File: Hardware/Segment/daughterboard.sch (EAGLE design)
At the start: 49 parts, among them IC1 PBQ79656PAPTQ1

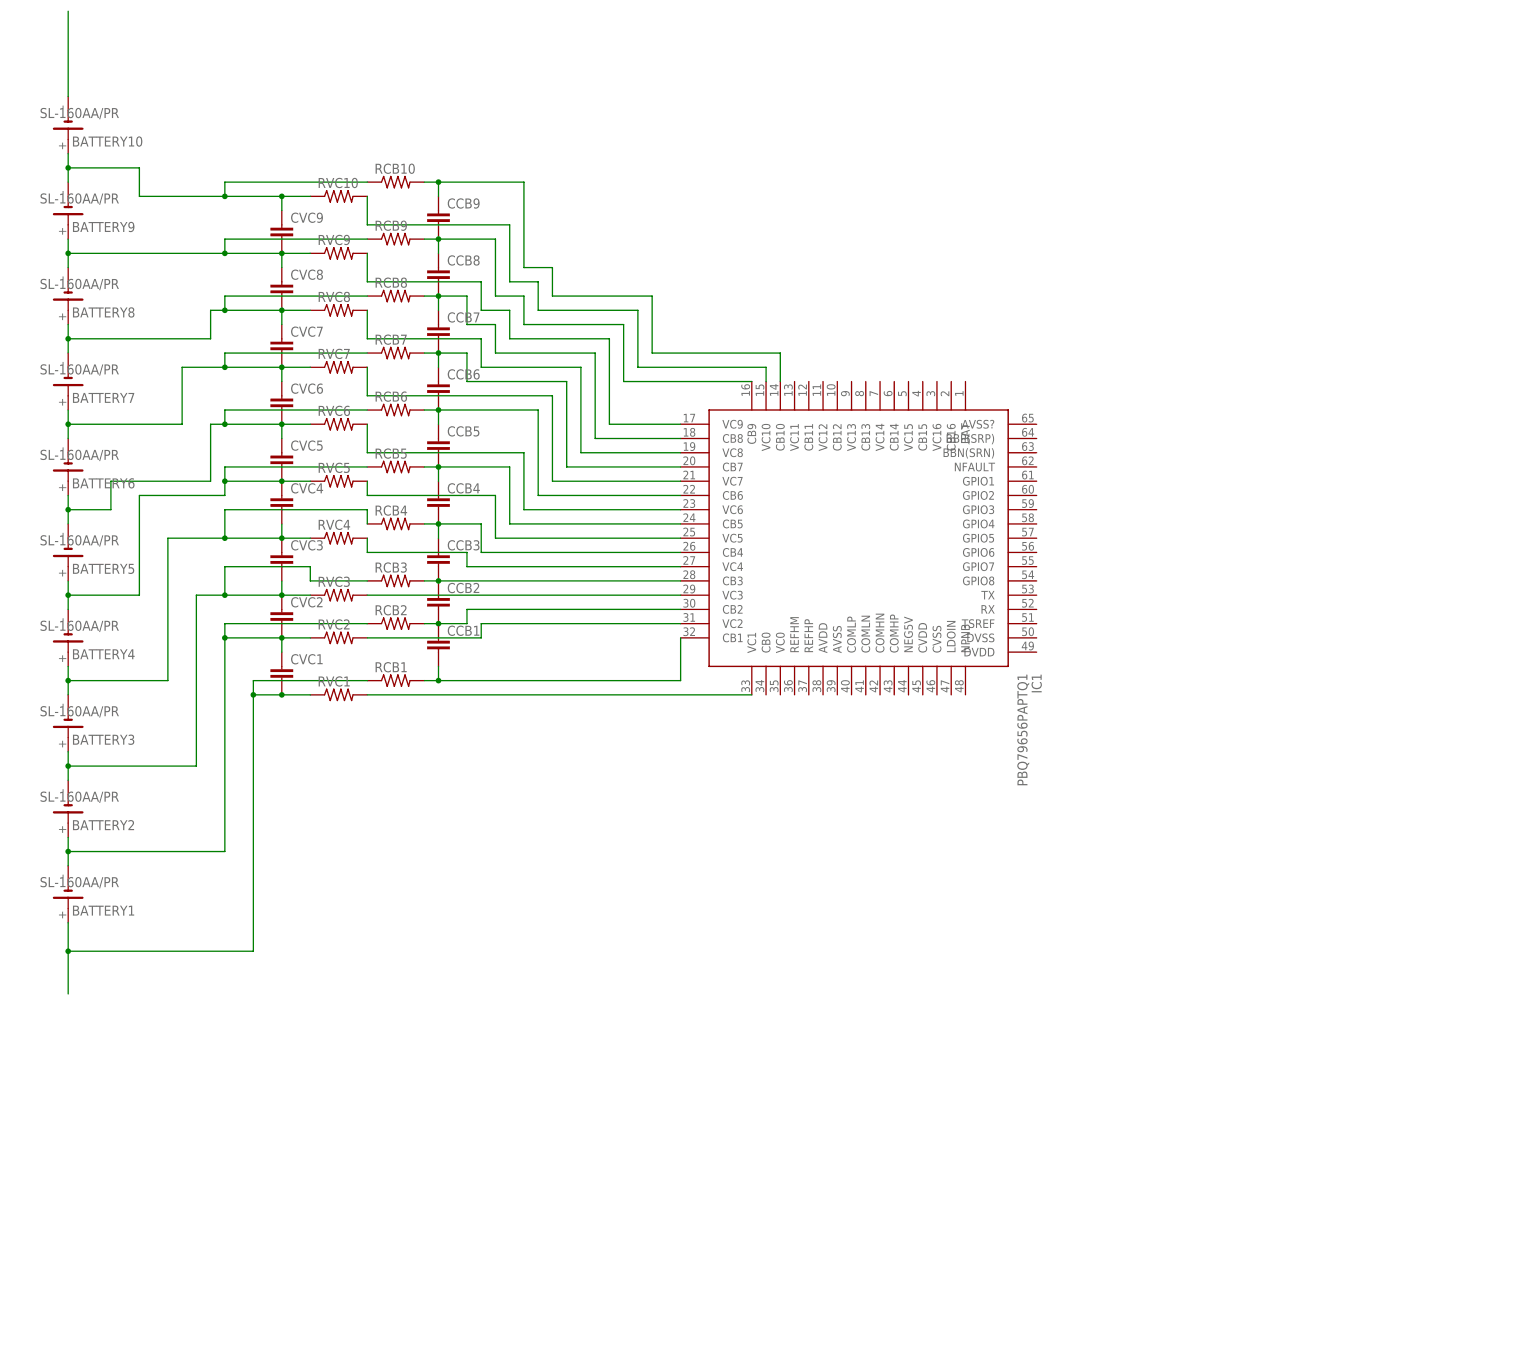
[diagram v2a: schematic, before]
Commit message: Added connections to thermistors
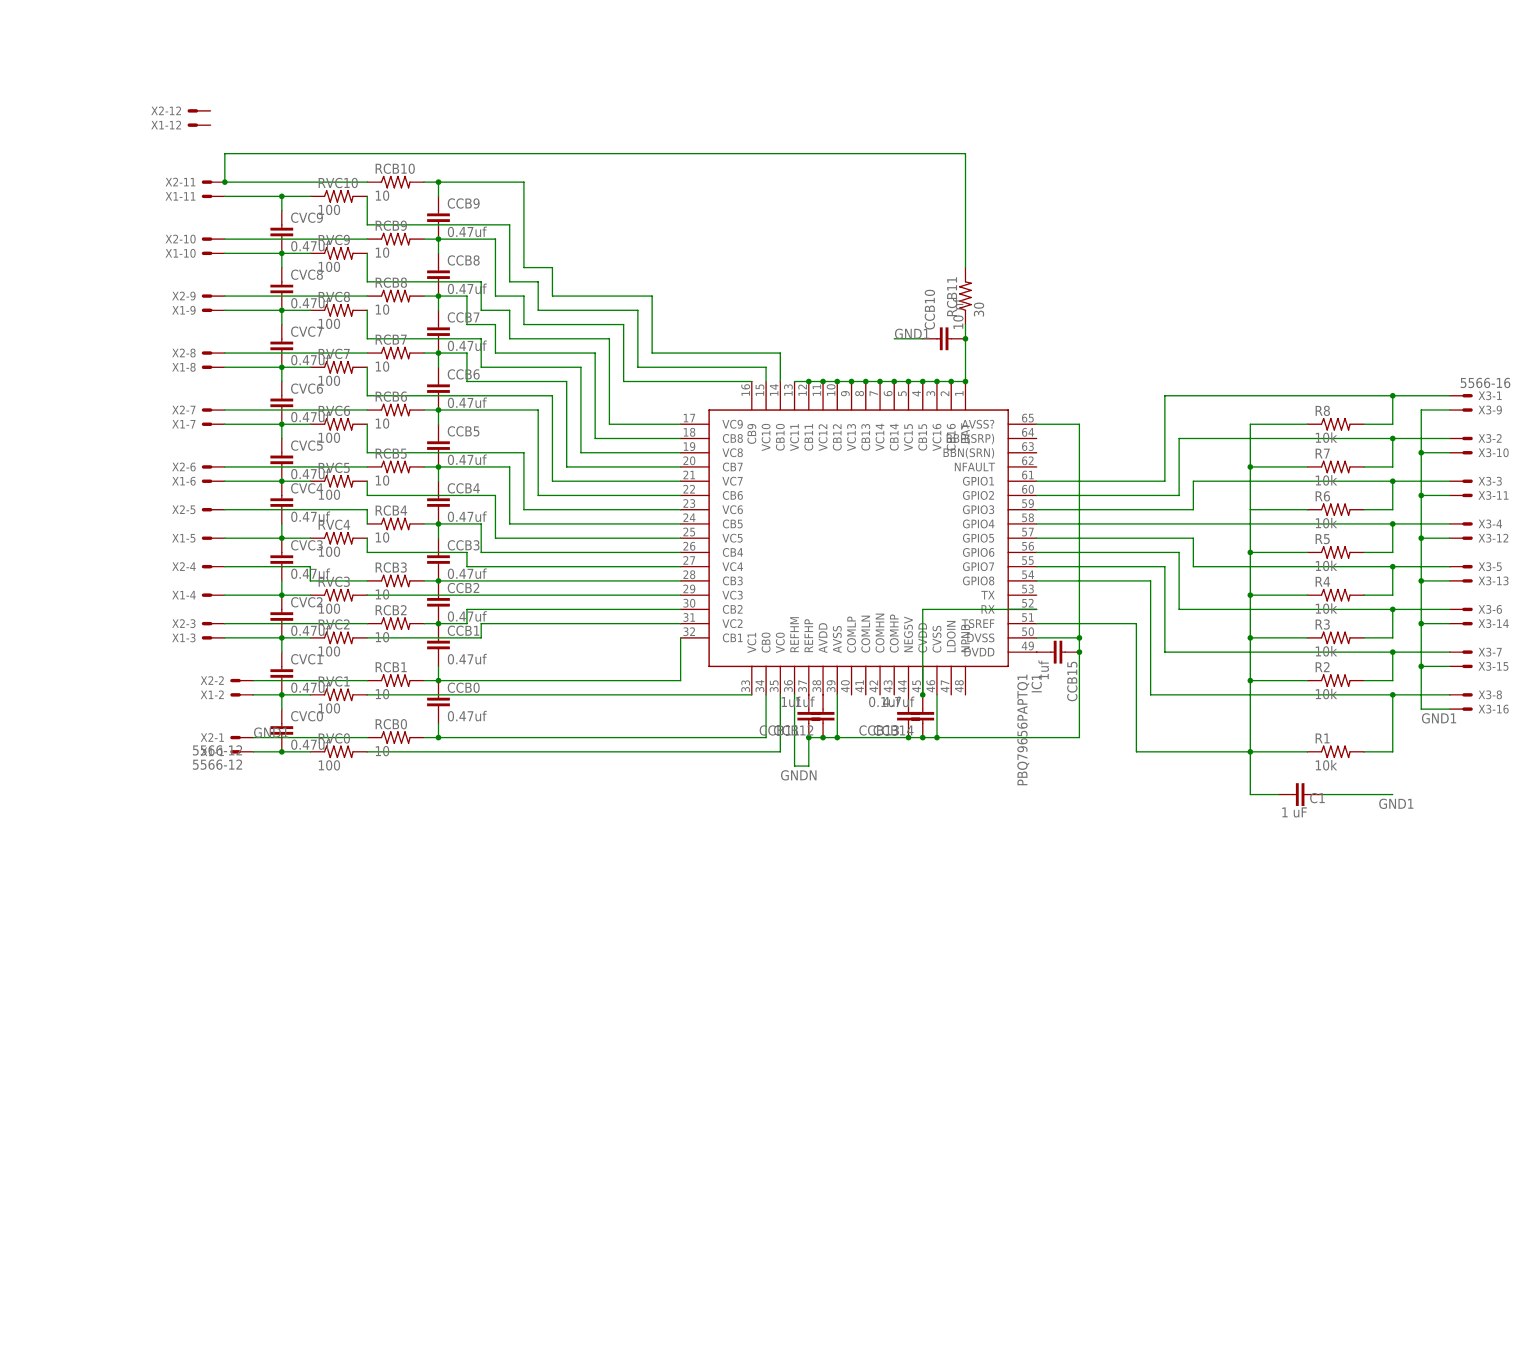
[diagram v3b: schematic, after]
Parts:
- removed BATTERY1, BATTERY10, BATTERY2, BATTERY3, BATTERY4, BATTERY5, BATTERY6, BATTERY7, BATTERY8, BATTERY9: SL-160AA/PR, battery:SL-160AA/PR
- added C1: 1 uF, capacitor-wima:C2.5/2
- added CCB0, CVC0: 0.47uf, capacitor-wima:C2.5/2
- added CCB10: 10 nf, capacitor-wima:C2.5/2
- added CCB11, CCB12, CCB15: 1uf, capacitor-wima:C2.5/2
- added CCB13: 0.1uf, capacitor-wima:C2.5/2
- added CCB14: 4.7uf, capacitor-wima:C2.5/2
- added R1, R2, R3, R4, R5, R6, R7, R8: 10k, rcl:R-US_R0603
- added RCB0: 10, rcl:R-US_R0603
- added RCB11: 30, rcl:R-US_R0603
- added RVC0: 100, rcl:R-US_R0603
- added X1, X2: 5566-12, con-molex:5566-12
- added X3: 5566-16, con-molex:5566-16
- CCB1, CCB2, CCB3, CCB4, CCB5, CCB6, CCB7, CCB8, CCB9, CVC1, CVC2, CVC3, CVC4, CVC5, CVC6, CVC7, CVC8, CVC9: value (none) -> 0.47uf
- RCB1, RCB10, RCB2, RCB3, RCB4, RCB5, RCB6, RCB7, RCB8, RCB9: value (none) -> 10
- RVC1, RVC10, RVC2, RVC3, RVC4, RVC5, RVC6, RVC7, RVC8, RVC9: value (none) -> 100
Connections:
- new net GND1: C1.1, CCB10.1, RCB0.1, X2-1.S, X3-10.S, X3-11.S, X3-12.S, X3-13.S, X3-14.S, X3-15.S, X3-16.S, X3-9.S
- new net GNDN: CCB11.1, CCB12.1, CCB13.1, CCB14.1, CCB15.1, IC1.AVSS, IC1.AVSS?, IC1.CVSS, IC1.DVSS, IC1.REFHM
- new net N$25: CCB0.2, IC1.CB0, RCB0.2
- new net N$33: CCB11.2, IC1.REFHP
- new net N$34: CVC0.2, RVC0.1, X1-1.S
- new net N$35: CVC0.1, CVC1.2, RVC1.1, X1-2.S
- new net N$36: CVC1.1, CVC2.2, RVC2.1, X1-3.S
- new net N$37: CVC2.1, CVC3.2, RVC3.1, X1-4.S
- new net N$38: CVC3.1, CVC4.2, RVC4.1, X1-5.S
- new net N$39: CVC4.1, CVC5.2, RVC5.1, X1-6.S
- new net N$40: CVC5.1, CVC6.2, RVC6.1, X1-7.S
- new net N$41: CVC6.1, CVC7.2, RVC7.1, X1-8.S
- new net N$42: CVC7.1, CVC8.2, RVC8.1, X1-9.S
- new net N$43: CVC8.1, CVC9.2, RVC9.1, X1-10.S
- new net N$44: CVC9.1, RVC10.1, X1-11.S
- new net N$45: CCB10.2, IC1.BAT, IC1.CB11, IC1.CB12, IC1.CB13, IC1.CB14, IC1.CB15, IC1.CB16, IC1.VC11, IC1.VC12, IC1.VC13, IC1.VC14, IC1.VC15, IC1.VC16, RCB11.1
- new net N$46: CCB12.2, IC1.AVDD
- new net N$47: IC1.GPIO1, R8.2, X3-1.S
- new net N$48: CCB13.2, IC1.NEG5V
- new net N$49: CCB14.2, IC1.CVDD, IC1.RX
- new net N$50: CCB15.2, IC1.DVDD
- new net N$51: IC1.GPIO2, R7.2, X3-2.S
- new net N$52: IC1.GPIO3, R6.2, X3-3.S
- new net N$53: IC1.GPIO4, R5.2, X3-4.S
- new net N$54: IC1.GPIO5, R4.2, X3-5.S
- new net N$55: IC1.GPIO6, R3.2, X3-6.S
- new net N$56: IC1.GPIO7, R2.2, X3-7.S
- new net N$57: IC1.GPIO8, R1.2, X3-8.S
- new net N$58: C1.2, IC1.TSREF, R1.1, R2.1, R3.1, R4.1, R5.1, R6.1, R7.1, R8.1
- net N$12: now also X2-5.S; no longer BATTERY3.-, BATTERY4.+, CVC3.1, CVC4.2, RVC4.1
- net N$15: now also X2-6.S; no longer BATTERY4.-, BATTERY5.+, CVC4.1, CVC5.2, RVC5.1
- net N$18: now also X2-9.S; no longer BATTERY7.-, BATTERY8.+, CVC7.1, CVC8.2, RVC8.1
- net N$2: now also CCB0.1
- net N$21: now also X2-10.S; no longer BATTERY8.-, BATTERY9.+, CVC8.1, CVC9.2, RVC9.1
- net N$24: now also IC1.VC0, RVC0.2; no longer BATTERY10.-
- net N$27: now also X2-7.S; no longer BATTERY5.-, BATTERY6.+, CVC5.1, CVC6.2, RVC6.1
- net N$29: now also RCB11.2, X2-11.S; no longer BATTERY10.+, BATTERY9.-, CVC9.1, RVC10.1
- net N$31: now also X2-8.S; no longer BATTERY6.-, BATTERY7.+, CVC6.1, CVC7.2, RVC7.1
- net N$5: now also X2-2.S; no longer BATTERY1.+, CVC1.2, RVC1.1
- net N$6: now also X2-3.S; no longer BATTERY1.-, BATTERY2.+, CVC1.1, CVC2.2, RVC2.1
- net N$8: now also X2-4.S; no longer BATTERY2.-, BATTERY3.+, CVC2.1, CVC3.2, RVC3.1

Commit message: Part of com
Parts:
- added CCB16, CCB17: 2.2nf, capacitor-wima:C2.5/2
- added CCB18, CCB19: 220pf, capacitor-wima:C2.5/2
- added RVC11, RVC12, RVC13, RVC14: 49, rcl:R-US_R0603
- added RVC15: 1k, rcl:R-US_R0603
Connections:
- new net N$59: CCB18.1, IC1.COMHN, RVC11.2, RVC15.2
- new net N$60: CCB19.2, IC1.COMHP, RVC12.2, RVC15.1
- new net N$61: CCB16.2, RVC11.1
- new net N$62: CCB17.2, RVC12.1
- new net N$63: CCB16.1, RVC13.2
- new net N$64: CCB17.1, RVC14.2
- net GNDN: now also CCB18.2, CCB19.1
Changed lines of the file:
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@@
 <part name="R7" library="rcl" library_urn="urn:adsk.eagle:library:334" deviceset="R-US_" device="R0603" package3d_urn="urn:adsk.eagle:package:23555/3" value="10k"/>
 <part name="R8" library="rcl" library_urn="urn:adsk.eagle:library:334" deviceset="R-US_" device="R0603" package3d_urn="urn:adsk.eagle:package:23555/3" value="10k"/>
+<part name="RVC11" library="rcl" library_urn="urn:adsk.eagle:library:334" deviceset="R-US_" device="R0603" package3d_urn="urn:adsk.eagle:package:23555/3" value="49"/>
+<part name="RVC12" library="rcl" library_urn="urn:adsk.eagle:library:334" deviceset="R-US_" device="R0603" package3d_urn="urn:adsk.eagle:package:23555/3" value="49"/>
+<part name="CCB16" library="capacitor-wima" library_urn="urn:adsk.eagle:library:116" deviceset="C" device="2.5/2" package3d_urn="urn:adsk.eagle:package:5415/1" value="2.2nf"/>
+<part name="CCB17" library="capacitor-wima" library_urn="urn:adsk.eagle:library:116" deviceset="C" device="2.5/2" package3d_urn="urn:adsk.eagle:package:5415/1" value="2.2nf"/>
+<part name="RVC13" library="rcl" library_urn="urn:adsk.eagle:library:334" deviceset="R-US_" device="R0603" package3d_urn="urn:adsk.eagle:package:23555/3" value="49"/>
+<part name="RVC14" library="rcl" library_urn="urn:adsk.eagle:library:334" deviceset="R-US_" device="R0603" package3d_urn="urn:adsk.eagle:package:23555/3" value="49"/>
+<part name="RVC15" library="rcl" library_urn="urn:adsk.eagle:library:334" deviceset="R-US_" device="R0603" package3d_urn="urn:adsk.eagle:package:23555/3" value="1k"/>
+<part name="CCB18" library="capacitor-wima" library_urn="urn:adsk.eagle:library:116" deviceset="C" device="2.5/2" package3d_urn="urn:adsk.eagle:package:5415/1" value="220pf"/>
+<part name="CCB19" library="capacitor-wima" library_urn="urn:adsk.eagle:library:116" deviceset="C" device="2.5/2" package3d_urn="urn:adsk.eagle:package:5415/1" value="220pf"/>
 </parts>
 <sheets>
@@
 <attribute name="NAME" x="240.03" y="77.6986" size="1.778" layer="95"/>
 <attribute name="VALUE" x="240.03" y="72.898" size="1.778" layer="96"/>
+</instance>
+<instance part="RVC11" gate="G$1" x="162.56" y="-2.54" smashed="yes" rot="R90">
+<attribute name="NAME" x="161.0614" y="-6.35" size="1.778" layer="95" rot="R90"/>
+<attribute name="VALUE" x="165.862" y="-6.35" size="1.778" layer="96" rot="R90"/>
+</instance>
+<instance part="RVC12" gate="G$1" x="165.1" y="-2.54" smashed="yes" rot="R90">
+<attribute name="NAME" x="163.6014" y="-6.35" size="1.778" layer="95" rot="R90"/>
+<attribute name="VALUE" x="168.402" y="-6.35" size="1.778" layer="96" rot="R90"/>
+</instance>
+<instance part="CCB16" gate="G$1" x="162.56" y="-12.7" smashed="yes" rot="R180">
+<attribute name="NAME" x="161.036" y="-13.081" size="1.778" layer="95" rot="R180"/>
+<attribute name="VALUE" x="161.036" y="-8.001" size="1.778" layer="96" rot="R180"/>
+</instance>
+<instance part="CCB17" gate="G$1" x="165.1" y="-12.7" smashed="yes" rot="R180">
+<attribute name="NAME" x="163.576" y="-13.081" size="1.778" layer="95" rot="R180"/>
+<attribute name="VALUE" x="163.576" y="-8.001" size="1.778" layer="96" rot="R180"/>
+</instance>
+<instance part="RVC13" gate="G$1" x="162.56" y="-20.32" smashed="yes" rot="R90">
+<attribute name="NAME" x="161.0614" y="-24.13" size="1.778" layer="95" rot="R90"/>
+<attribute name="VALUE" x="165.862" y="-24.13" size="1.778" layer="96" rot="R90"/>
+</instance>
+<instance part="RVC14" gate="G$1" x="165.1" y="-20.32" smashed="yes" rot="R90">
+<attribute name="NAME" x="163.6014" y="-24.13" size="1.778" layer="95" rot="R90"/>
+<attribute name="VALUE" x="168.402" y="-24.13" size="1.778" layer="96" rot="R90"/>
+</instance>
+<instance part="RVC15" gate="G$1" x="165.1" y="5.08" smashed="yes" rot="R180">
+<attribute name="NAME" x="168.91" y="3.5814" size="1.778" layer="95" rot="R180"/>
+<attribute name="VALUE" x="168.91" y="8.382" size="1.778" layer="96" rot="R180"/>
+</instance>
+<instance part="CCB18" gate="G$1" x="160.02" y="7.62" smashed="yes" rot="R270">
+<attribute name="NAME" x="160.401" y="6.096" size="1.778" layer="95" rot="R270"/>
+<attribute name="VALUE" x="155.321" y="6.096" size="1.778" layer="96" rot="R270"/>
+</instance>
+<instance part="CCB19" gate="G$1" x="170.18" y="7.62" smashed="yes" rot="R270">
+<attribute name="NAME" x="170.561" y="6.096" size="1.778" layer="95" rot="R270"/>
+<attribute name="VALUE" x="165.481" y="6.096" size="1.778" layer="96" rot="R270"/>
 </instance>
 </instances>
@@
 <wire x1="198.12" y1="38.1" x2="198.12" y2="35.56" width="0.1524" layer="91"/>
 <wire x1="198.12" y1="35.56" x2="198.12" y2="20.32" width="0.1524" layer="91"/>
-<wire x1="198.12" y1="20.32" x2="172.72" y2="20.32" width="0.1524" layer="91"/>
+<wire x1="198.12" y1="20.32" x2="175.26" y2="20.32" width="0.1524" layer="91"/>
 <junction x="198.12" y="35.56"/>
 <junction x="172.72" y="20.32"/>
 <pinref part="IC1" gate="G$1" pin="AVSS?"/>
+<wire x1="175.26" y1="20.32" x2="172.72" y2="20.32" width="0.1524" layer="91"/>
 <wire x1="190.5" y1="76.2" x2="198.12" y2="76.2" width="0.1524" layer="91"/>
 <wire x1="198.12" y1="76.2" x2="198.12" y2="38.1" width="0.1524" layer="91"/>
 <junction x="198.12" y="38.1"/>
+<pinref part="CCB18" gate="G$1" pin="2"/>
+<wire x1="154.94" y1="7.62" x2="154.94" y2="10.16" width="0.1524" layer="91"/>
+<pinref part="CCB19" gate="G$1" pin="1"/>
+<wire x1="154.94" y1="10.16" x2="172.72" y2="10.16" width="0.1524" layer="91"/>
+<wire x1="172.72" y1="10.16" x2="172.72" y2="7.62" width="0.1524" layer="91"/>
+<wire x1="172.72" y1="7.62" x2="175.26" y2="7.62" width="0.1524" layer="91"/>
+<wire x1="175.26" y1="7.62" x2="175.26" y2="20.32" width="0.1524" layer="91"/>
+<junction x="172.72" y="7.62"/>
+<junction x="175.26" y="20.32"/>
 </segment>
 </net>
@@
 </segment>
 </net>
+<net name="N$59" class="0">
+<segment>
+<pinref part="IC1" gate="G$1" pin="COMHN"/>
+<wire x1="162.56" y1="27.94" x2="162.56" y2="7.62" width="0.1524" layer="91"/>
+<pinref part="RVC11" gate="G$1" pin="2"/>
+<pinref part="RVC15" gate="G$1" pin="2"/>
+<wire x1="162.56" y1="7.62" x2="162.56" y2="2.54" width="0.1524" layer="91"/>
+<wire x1="160.02" y1="5.08" x2="160.02" y2="7.62" width="0.1524" layer="91"/>
+<wire x1="160.02" y1="7.62" x2="162.56" y2="7.62" width="0.1524" layer="91"/>
+<junction x="162.56" y="7.62"/>
+<pinref part="CCB18" gate="G$1" pin="1"/>
+</segment>
+</net>
+<net name="N$60" class="0">
+<segment>
+<pinref part="IC1" gate="G$1" pin="COMHP"/>
+<wire x1="165.1" y1="27.94" x2="165.1" y2="7.62" width="0.1524" layer="91"/>
+<pinref part="RVC12" gate="G$1" pin="2"/>
+<pinref part="RVC15" gate="G$1" pin="1"/>
+<wire x1="165.1" y1="7.62" x2="165.1" y2="2.54" width="0.1524" layer="91"/>
+<wire x1="170.18" y1="5.08" x2="170.18" y2="7.62" width="0.1524" layer="91"/>
+<wire x1="170.18" y1="7.62" x2="165.1" y2="7.62" width="0.1524" layer="91"/>
+<junction x="165.1" y="7.62"/>
+<pinref part="CCB19" gate="G$1" pin="2"/>
+</segment>
+</net>
+<net name="N$61" class="0">
+<segment>
+<pinref part="CCB16" gate="G$1" pin="2"/>
+<pinref part="RVC11" gate="G$1" pin="1"/>
+</segment>
+</net>
+<net name="N$62" class="0">
+<segment>
+<pinref part="CCB17" gate="G$1" pin="2"/>
+<pinref part="RVC12" gate="G$1" pin="1"/>
+</segment>
+</net>
+<net name="N$63" class="0">
+<segment>
+<pinref part="RVC13" gate="G$1" pin="2"/>
+<pinref part="CCB16" gate="G$1" pin="1"/>
+</segment>
+</net>
+<net name="N$64" class="0">
+<segment>
+<pinref part="RVC14" gate="G$1" pin="2"/>
+<pinref part="CCB17" gate="G$1" pin="1"/>
+</segment>
+</net>
